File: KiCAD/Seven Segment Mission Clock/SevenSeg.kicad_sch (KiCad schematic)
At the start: 36 parts, among them J201 Input, J202 Output, U201 AZ1117-5.0

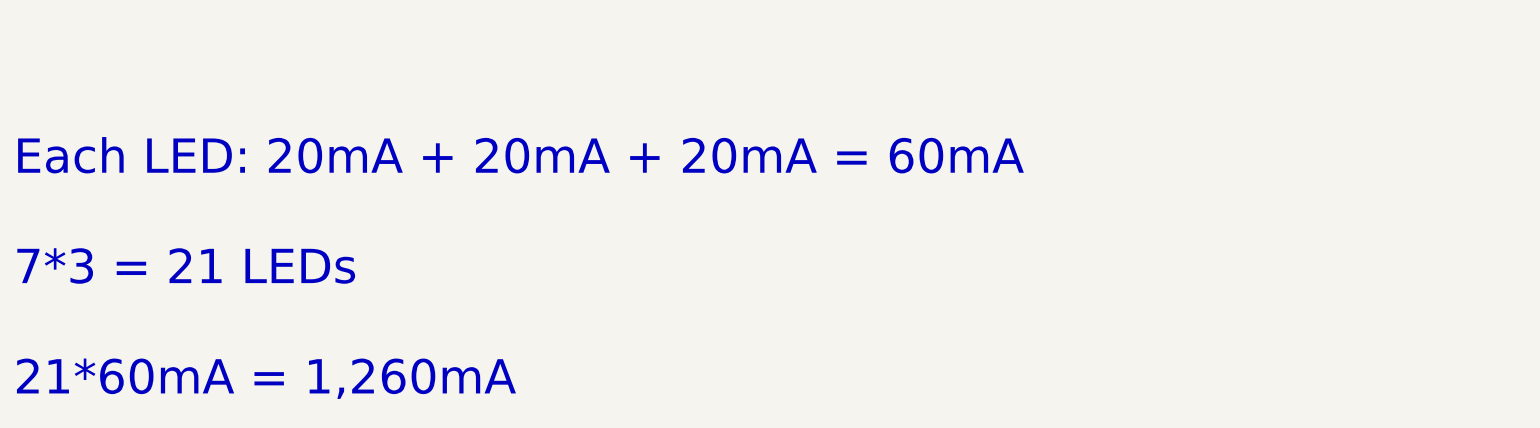
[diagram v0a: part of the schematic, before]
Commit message: Created Sixteen Segment Schematic
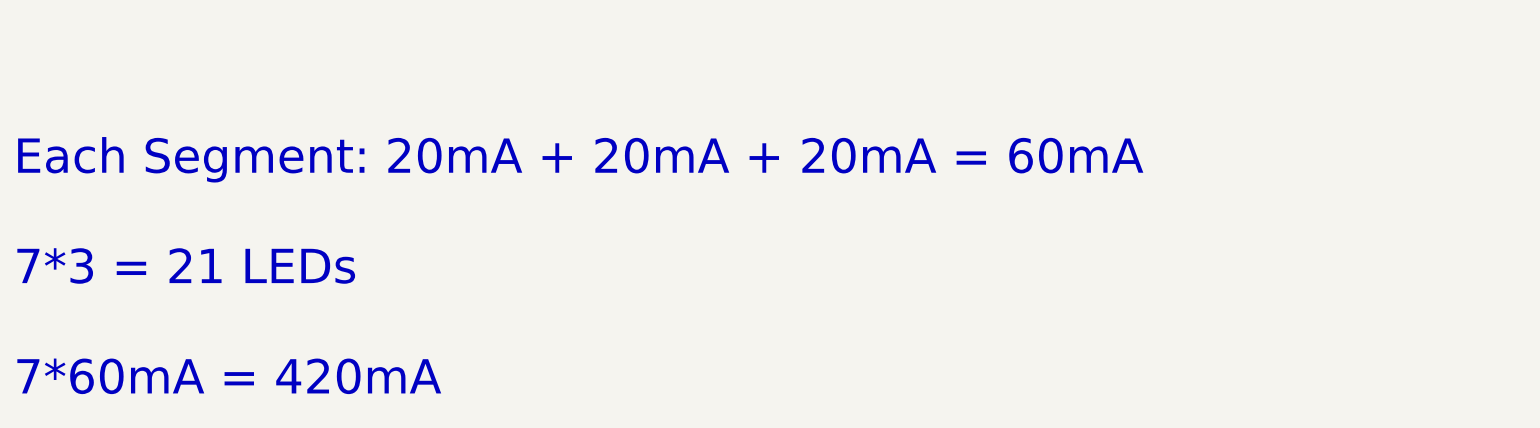
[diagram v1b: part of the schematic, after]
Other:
- note added: "Each Segment: 20mA + 20mA + 20mA = 60mA 7*3 = 21 LEDs 7*60mA = 420mA"
- note removed: "Each LED: 20mA + 20mA + 20mA = 60mA 7*3 = 21 LEDs 21*60mA = 1,260mA"
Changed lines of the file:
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@@
     (effects (font (size 3.81 3.81)) (justify left bottom))
   )
-  (text "Each LED: 20mA + 20mA + 20mA = 60mA\n\n7*3 = 21 LEDs\n\n21*60mA = 1,260mA"
+  (text "Each Segment: 20mA + 20mA + 20mA = 60mA\n\n7*3 = 21 LEDs\n\n7*60mA = 420mA"
     (at 16.51 247.65 0)
     (effects (font (size 5.08 5.08)) (justify left bottom))

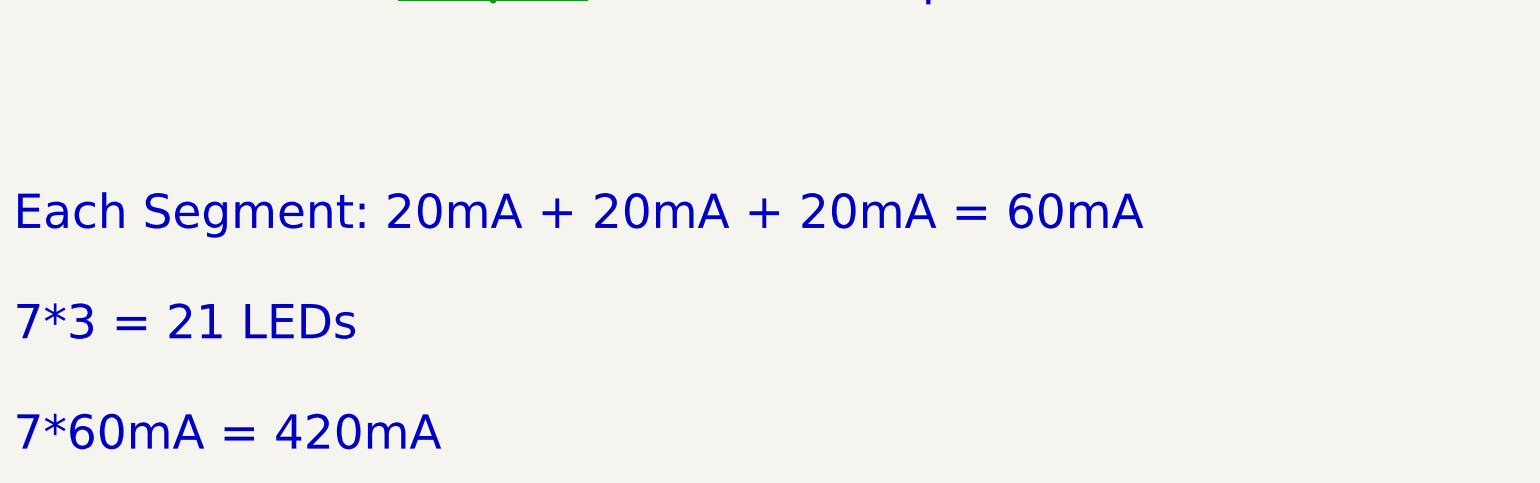
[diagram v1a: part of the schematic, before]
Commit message: Fixed regulator math, added to sixteen segment display
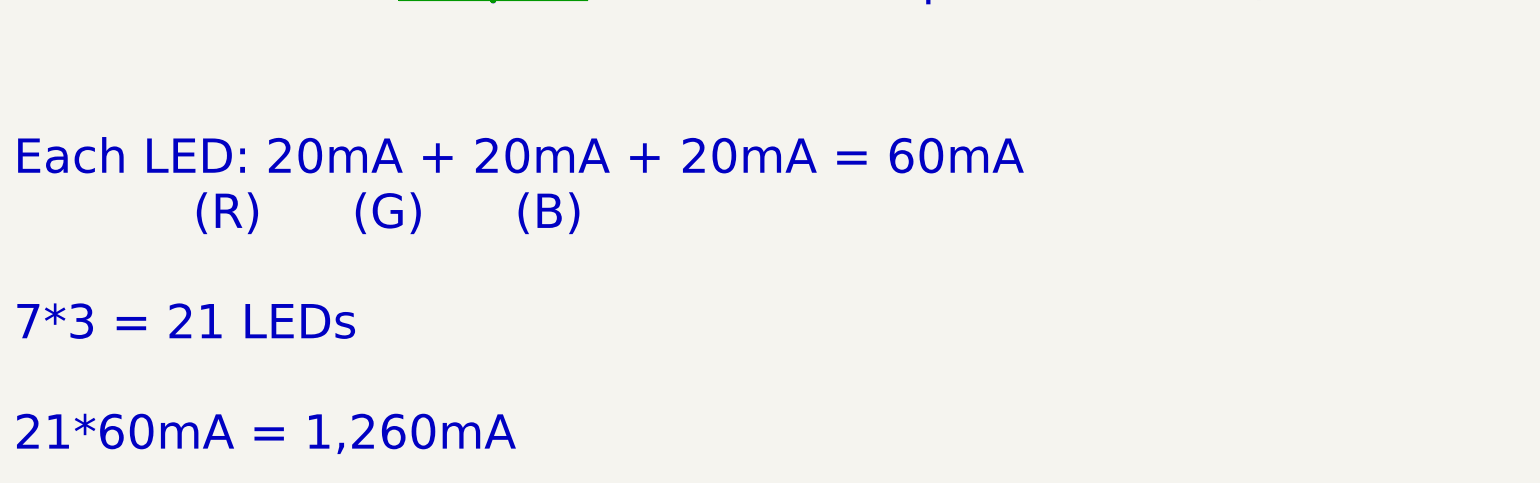
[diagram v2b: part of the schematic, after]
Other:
- note added: "Each LED: 20mA + 20mA + 20mA = 60mA (R) (G) (B) 7*3 = 21 LEDs 21*60mA = 1,260mA"
- note removed: "Each Segment: 20mA + 20mA + 20mA = 60mA 7*3 = 21 LEDs 7*60mA = 420mA"
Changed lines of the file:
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@@
     (effects (font (size 3.81 3.81)) (justify left bottom))
   )
-  (text "Each Segment: 20mA + 20mA + 20mA = 60mA\n\n7*3 = 21 LEDs\n\n7*60mA = 420mA"
+  (text "Each LED: 20mA + 20mA + 20mA = 60mA\n            (R)      (G)      (B)\n\n7*3 = 21 LEDs\n\n21*60mA = 1,260mA"
     (at 16.51 247.65 0)
     (effects (font (size 5.08 5.08)) (justify left bottom))
